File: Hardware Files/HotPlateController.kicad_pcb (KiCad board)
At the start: 2 copper layers, 75 x 75 mm, 40 parts, among them J1 Conn_01x02, J2 0.100" 2x4 Header, J3 Screw_Terminal_01x03, J4 Screw_Terminal_01x03, J6 Conn_01x02, M1 Conn_01x01, M2 Conn_01x01, M3 Conn_01x01, M4 Conn_01x01, Q1 NMOS 60V 300mA, Q2 NMOS 60V 3A, SW1 SPST, SW2 SPST, U1 NCP1117ST33T3G, U2 ACS712xLCTR-20A, U3 ESP32-WROOM-32, U4 MAX31855KASA

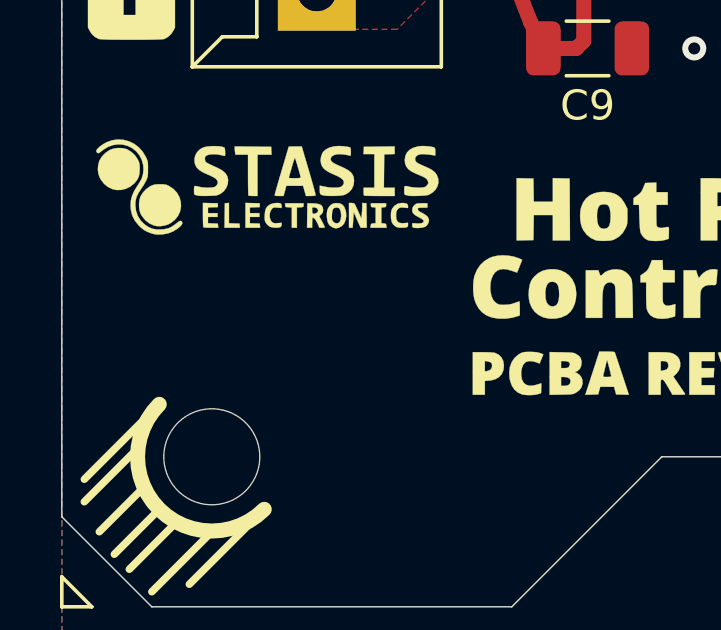
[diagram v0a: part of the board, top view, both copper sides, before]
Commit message: add jlcpcb ordering number
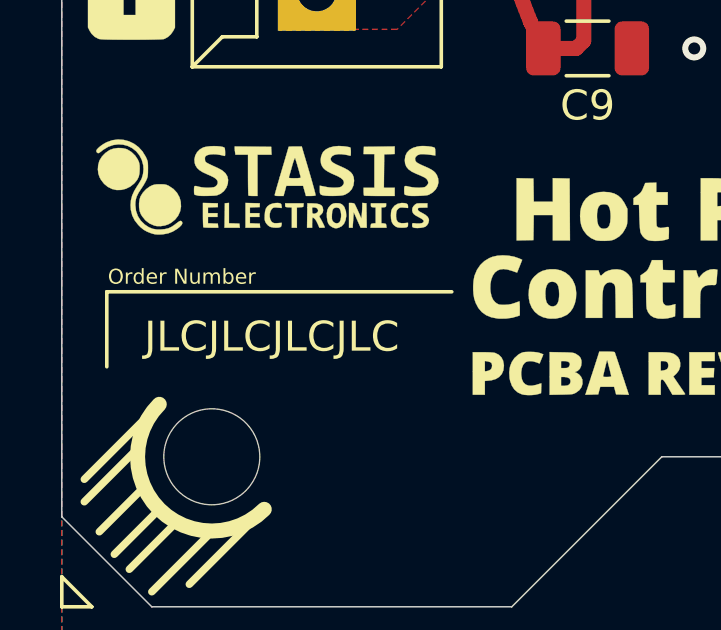
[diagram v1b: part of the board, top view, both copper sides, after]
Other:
- board text added: "JLCJLCJLCJLC"
- board text added: "Order Number"
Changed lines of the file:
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@@
   (general
     (thickness 1.6)
-    (drawings 72)
+    (drawings 76)
     (tracks 266)
     (zones 0)
@@
     (32 B.Adhes user hide)
     (33 F.Adhes user hide)
-    (34 B.Paste user hide)
+    (34 B.Paste user)
     (35 F.Paste user hide)
     (36 B.SilkS user hide)
@@
     )
   )
+  (gr_line (start 1.5 64.5) (end 13 64.5) (layer F.SilkS) (width 0.12))
+  (gr_line (start 1.5 67) (end 1.5 64.5) (layer F.SilkS) (width 0.12))
+  (gr_text "Order Number" (at 4 64) (layer F.SilkS)
+    (effects (font (size 0.5 0.5) (thickness 0.1)))
+  )
+  (gr_text JLCJLCJLCJLC (at 7 66) (layer F.SilkS)
+    (effects (font (size 1 1) (thickness 0.15)))
+  )
   (gr_line (start 69.75 72.5) (end 71.5 74.25) (layer F.SilkS) (width 0.25))

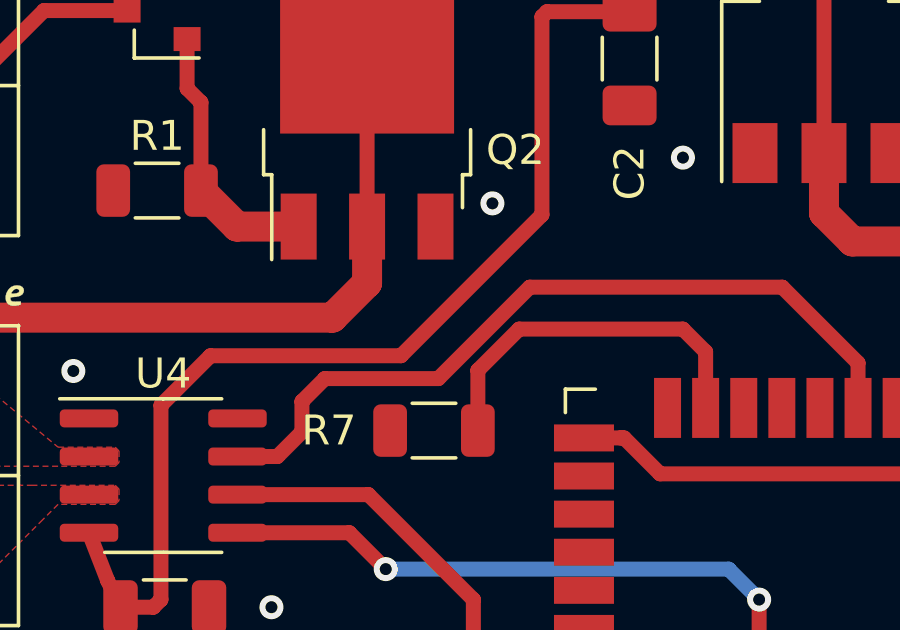
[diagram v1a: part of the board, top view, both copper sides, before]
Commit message: Fix missing hot plate control trace
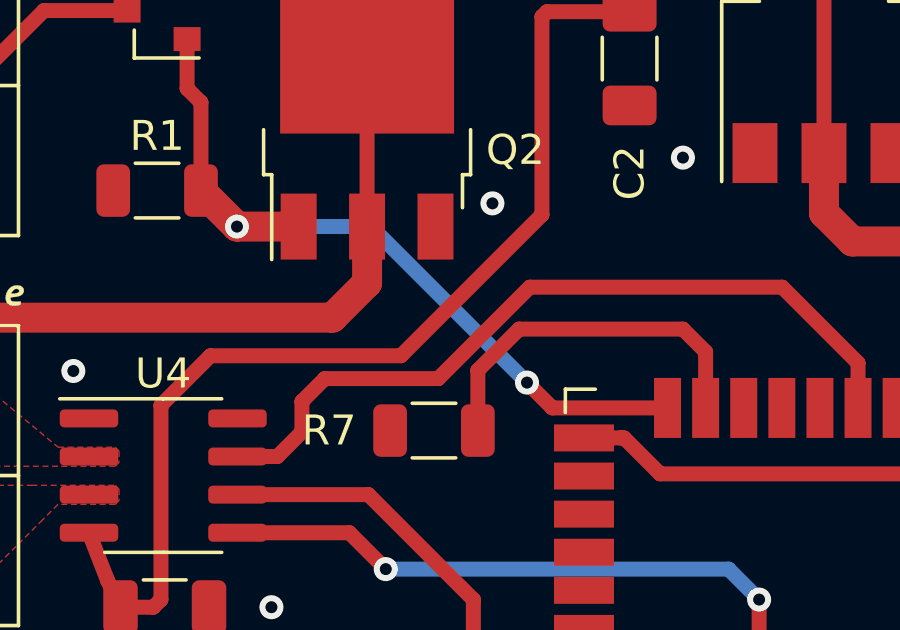
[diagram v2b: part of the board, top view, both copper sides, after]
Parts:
- removed the G*** at (37.5, 37.5)
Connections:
- U3 pad 24: Net-(U3-Pad24) -> PlateControl
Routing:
- net PlateControl: track 9.00 -> 25.9 mm, vias 0 -> 2

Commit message: Reroute Thermocouple IC traces
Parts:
- moved R7 11.6 mm to (37.0, 45.6), turned to 0 degrees
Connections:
- U3 pad 19: /ESP32_SPI_MISO -> Net-(U3-Pad19)
- U3 pad 29: Net-(U3-Pad29) -> /ESP32_SPI_SCK
- U3 pad 31: Net-(U3-Pad31) -> /ESP32_SPI_MISO
- U3 pad 5: /ESP32_SPI_SCK -> Net-(U3-Pad5)
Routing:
- net /ESP32_SPI_SCK: track 36.9 -> 18.9 mm
- net /ESP32_SPI_MISO: track 26.2 -> 15.1 mm
- net U0TX_Active: track 12.4 -> 4.15 mm

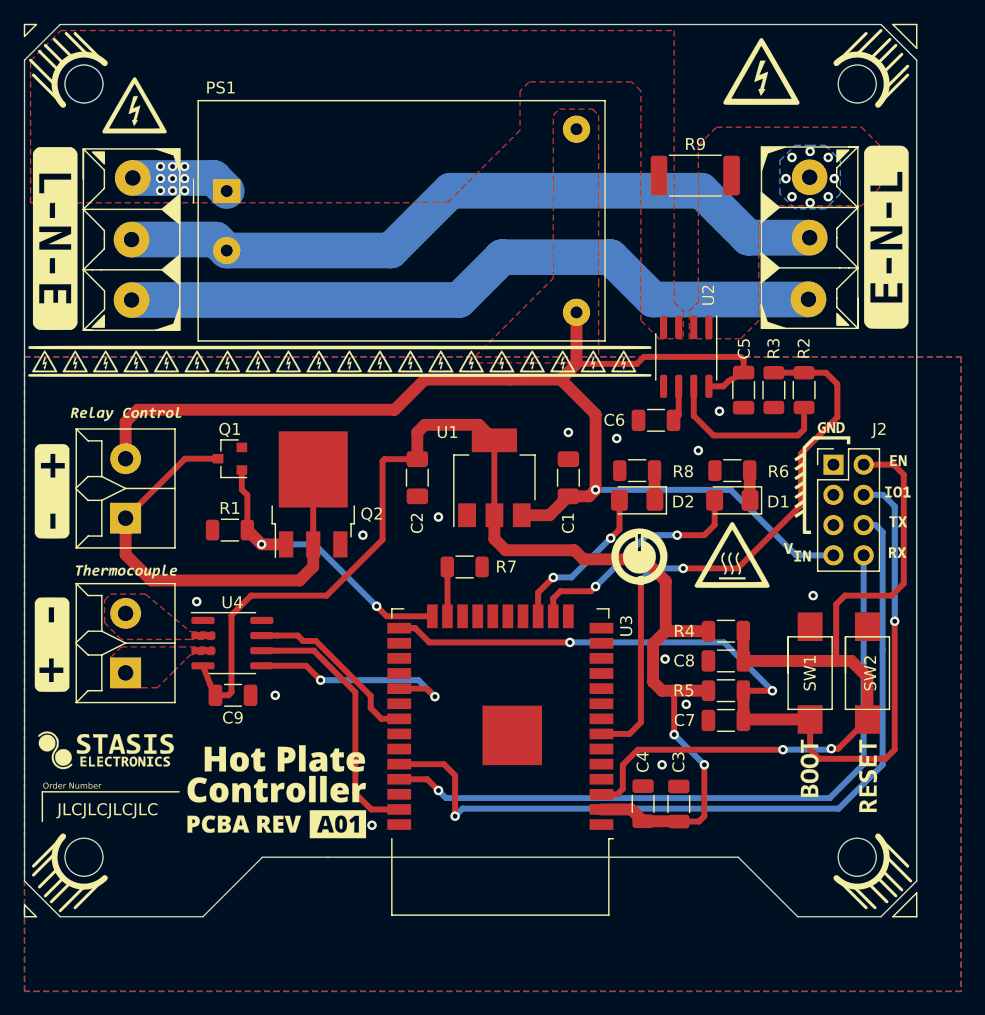
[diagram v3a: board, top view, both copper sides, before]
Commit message: Fix Thermocouple layout adjust pinouts to fix GPIO Issues adjust schematic formatting
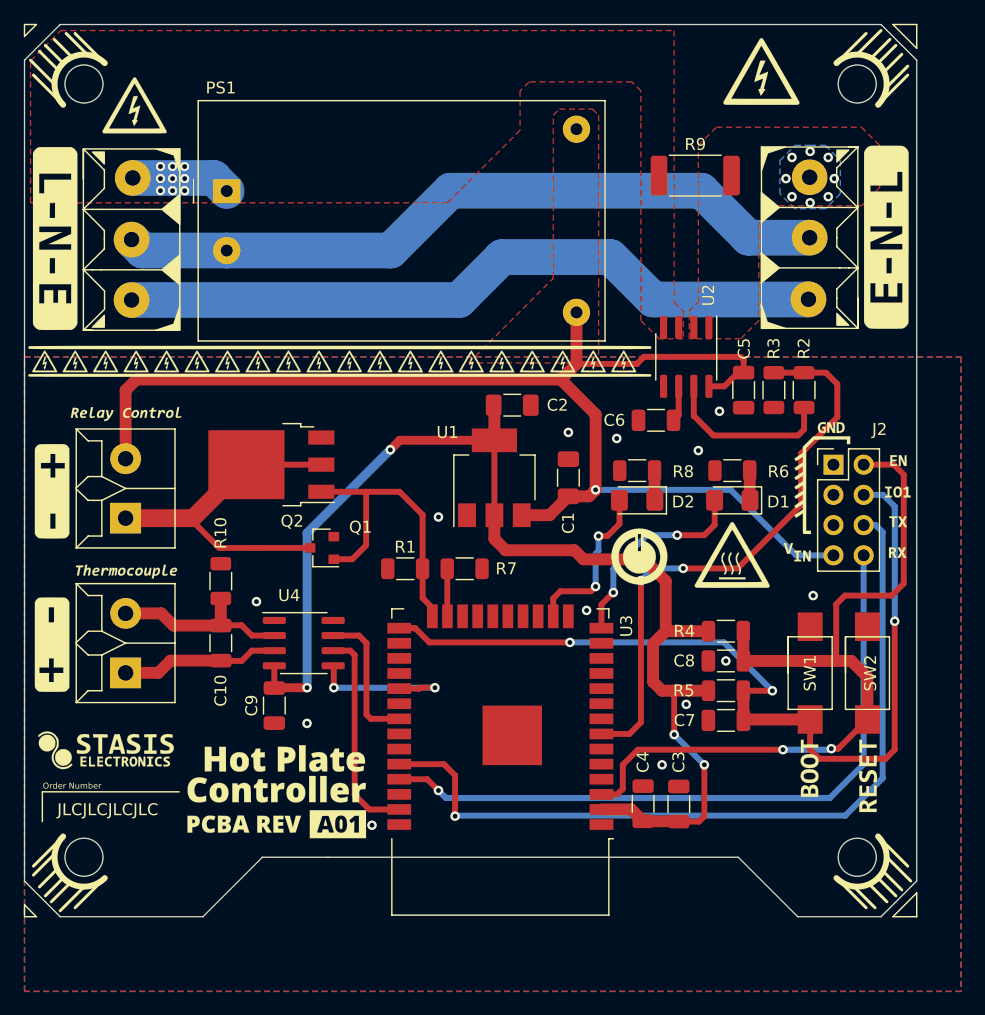
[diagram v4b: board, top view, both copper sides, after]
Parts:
- added C10: 10nF 50V, Capacitor_SMD:C_1206_3216Metric, F.Cu at (16.5, 52.0)
- added R10: 0R, Resistor_SMD:R_1206_3216Metric, F.Cu at (16.5, 46.8)
- moved R1 15.1 mm to (32.0, 45.8)
- moved Q1 10.8 mm to (25.0, 44.0)
- moved C2 10.0 mm to (41.0, 32.0), turned to 0 degrees
- moved U4 6.00 mm to (23.5, 52.0)
- moved Q2 4.32 mm to (20.8, 37.0), turned to 180 degrees
- moved C9 3.58 mm to (21.0, 57.2), turned to 270 degrees
- moved R7 0.15 mm to (37.0, 45.8)
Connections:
- net Net-(J3-Pad1) renamed AC_Line_Out
- net Net-(J3-Pad2) renamed AC_Neutral
- net Net-(J4-Pad3) renamed AC_Line_In
- net V_Current renamed Net-(R2-Pad1)
- U3 pad 14: Net-(U3-Pad14) -> StatusLED
- U3 pad 16: StatusLED -> HotLED
- U3 pad 17: HotLED -> Net-(U3-Pad17)
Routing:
- net Net-(C10-Pad2): track 0.00 -> 15.6 mm
- net Net-(C10-Pad1): track 0.00 -> 13.3 mm
- net +3V3: track 107.6 -> 102.1 mm, vias 2 -> 4
- net /ESP32_SPI_SCK: track 18.9 -> 13.5 mm
- net /ESP32_SPI_TEMPSENSOR_1_CS: track 22.1 -> 18.0 mm
- net Net-(J1-Pad1): track 38.2 -> 34.8 mm
- net /ESP32_SPI_MISO: track 15.1 -> 12.0 mm
- net StatusLED: track 19.7 -> 17.5 mm
- net +5V: track 105.9 -> 107.6 mm
- net /USB_TX: track 67.6 -> 68.3 mm
- net HotLED: track 13.5 -> 14.0 mm
- net PlateControl: vias 2 -> 0
- removed copper zone on F.Cu, net Net-(C10-Pad1)
- removed copper zone on F.Cu, net Net-(C10-Pad2)

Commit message: add 5v sense circuit Move around components Adjust board shape
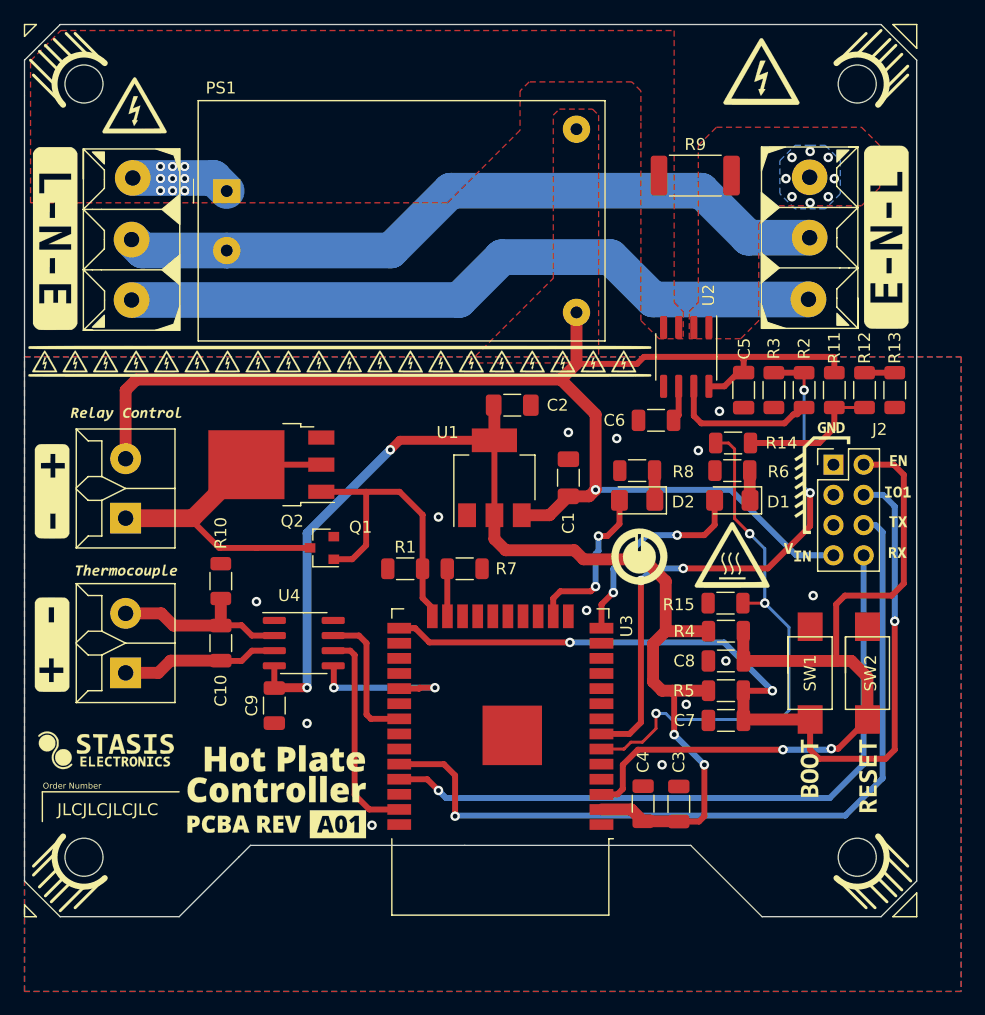
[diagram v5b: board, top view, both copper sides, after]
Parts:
- added R11: 1.37k 0.25W 1%, Resistor_SMD:R_1206_3216Metric, F.Cu at (68.1, 30.7)
- added R12: 1.37k 0.25W 1%, Resistor_SMD:R_1206_3216Metric, F.Cu at (70.6, 30.7)
- added R13: 1.37k 0.25W 1%, Resistor_SMD:R_1206_3216Metric, F.Cu at (73.2, 30.7)
- added R14: 1.37k 0.25W 1%, Resistor_SMD:R_1206_3216Metric, F.Cu at (59.6, 35.2)
- added R15: 2.67k 0.25W 1%, Resistor_SMD:R_1206_3216Metric, F.Cu at (58.9, 48.6)
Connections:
- net /EN renamed EN
- net /ESP32_SPI_MISO renamed ESP32_SPI_MISO
- net /ESP32_SPI_SCK renamed ESP32_SPI_SCK
- net /ESP32_SPI_TEMPSENSOR_1_CS renamed ESP32_SPI_TEMPSENSOR_1_CS
- net /USB_RX renamed USB_RX
- net /USB_TX renamed USB_TX
- net UserSwitch renamed IO0
- U3 pad 6: Net-(U3-Pad6) -> 5V_Current_adj
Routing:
- net 5V_Current_adj: track 0.00 -> 45.8 mm, vias 0 -> 3
- net Net-(R11-Pad2): track 0.00 -> 11.8 mm
- net +5V: track 107.6 -> 116.8 mm
- net Net-(R12-Pad2): track 0.00 -> 2.54 mm
- net Net-(R2-Pad1): track 14.5 -> 12.8 mm
- net V_Current_adj: track 48.9 -> 47.5 mm, vias 2 -> 4
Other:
- outline, holes or cut-outs redrawn

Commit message: Finalize Layout Finalize Artwork Finalize Schematic
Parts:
- moved G*** 3.22 mm to (37.5, 37.5)
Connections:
- net 5V_Current_adj renamed 5V_adj
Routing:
- net IO0: track 77.9 -> 83.5 mm

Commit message: add bottom artwork add part info to missing 10nF cap update BOM
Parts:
- added G***: LOGO, HotPlateController:silkscreenart_bottom, B.Cu at (37.5, 37.5)
